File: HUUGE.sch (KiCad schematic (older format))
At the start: 16 parts

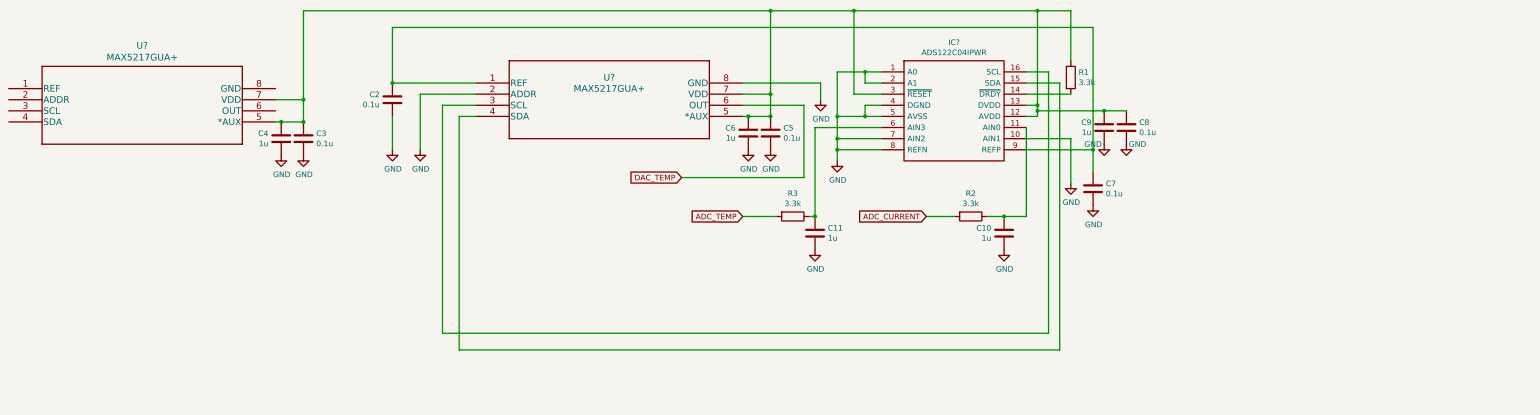
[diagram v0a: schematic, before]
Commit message: finish big sch + add appropriate labels
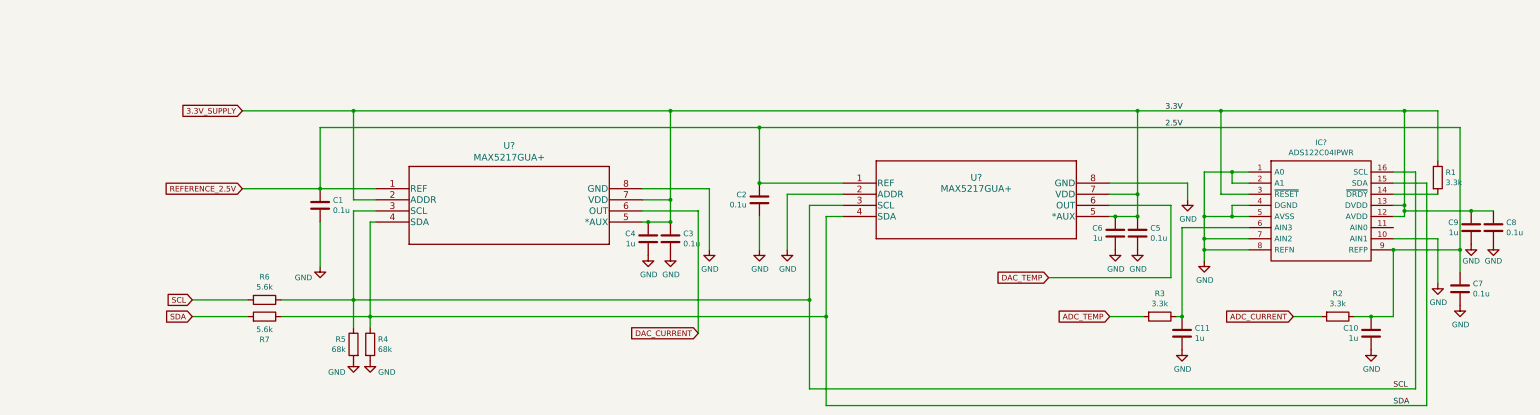
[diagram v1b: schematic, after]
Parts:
- added C1: 0.1u, symbol Device:C
- added R4, R5: 68k, symbol Device:R
- added R6, R7: 5.6k, symbol Device:R
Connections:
- net GND: now also U?.8 (GND), C1.2, R4.2, R5.2
- net REFERENCE_2.5V: now reaches C10.1, R2.1
- net REFERENCE_2.5V: now also C2.1, C7.1, IC?.9 (REFP), U?.1 (REF), U?.1 (REF), C1.1; no longer IC?.11 (AIN0)
- net 3.3V_SUPPLY: now reaches C3.1, C4.1, C5.1, C6.1, C8.1, C9.1, IC?.12 (AVDD), IC?.13 (DVDD), IC?.3 (~RESET), R1.1, U?.5 (*AUX), U?.5 (*AUX), U?.7 (VDD), U?.7 (VDD)
- net 3.3V_SUPPLY: now also U?.2 (ADDR)
- net SDA: now reaches IC?.15 (SDA), U?.4 (SDA)
- net SDA: now also U?.4 (SDA), R4.1, R7.1, R7.2
- net SCL: now reaches IC?.16 (SCL), U?.3 (SCL)
- net SCL: now also U?.3 (SCL), R5.1, R6.1, R6.2
- net DAC_CURRENT: now reaches U?.6 (OUT)
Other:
- moved on the sheet: C10, C11, C2, C3, C4, C5, C6, C7, C8, C9, IC?, R1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

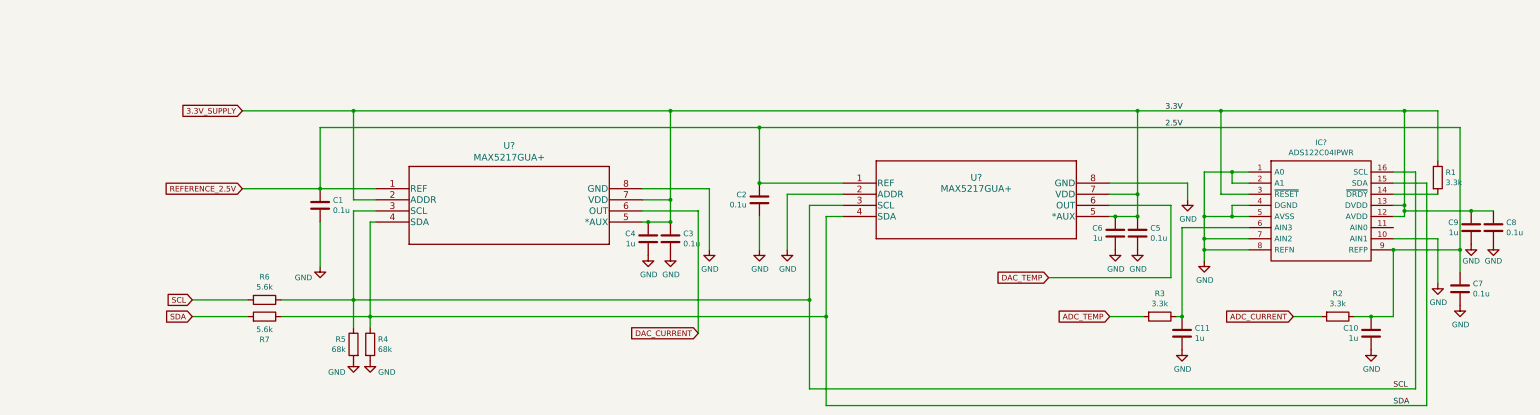
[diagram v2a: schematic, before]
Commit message: annotate all sheets
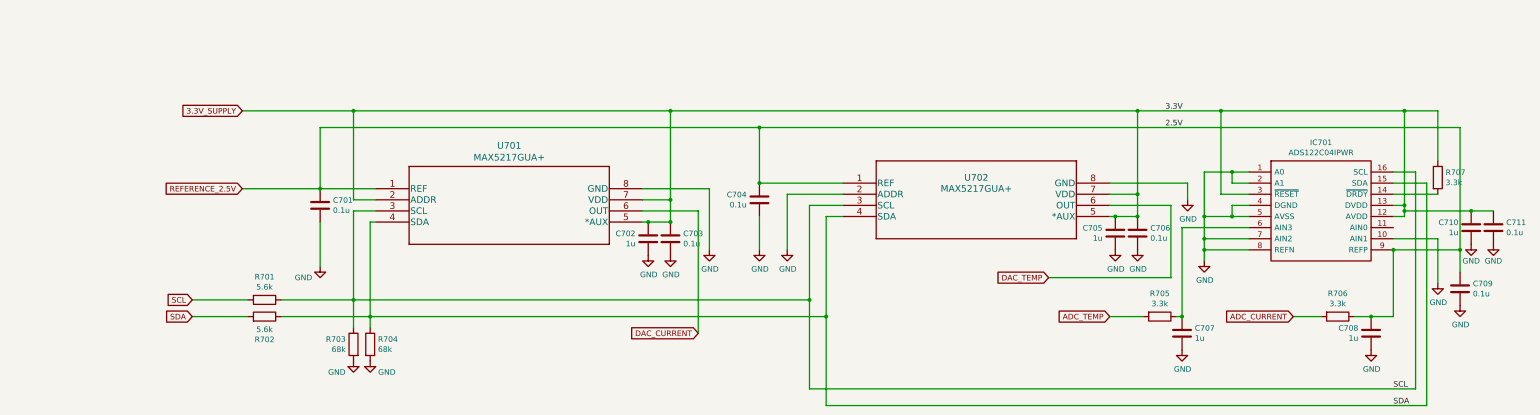
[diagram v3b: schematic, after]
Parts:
- gave numbers to parts that had none: 3
- renumbered C1 to C701, C4 to C702, C3 to C703, C2 to C704, C6 to C705, C5 to C706, C11 to C707, C10 to C708, C7 to C709, C9 to C710, C8 to C711, R6 to R701, R7 to R702, R5 to R703, R4 to R704, R3 to R705, R2 to R706, R1 to R707
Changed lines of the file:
@@
 $EndDescr
 $Comp
-L ADS122C04IPWR:ADS122C04IPWR IC?
+L ADS122C04IPWR:ADS122C04IPWR IC701
 U 1 1 60C9892C
 P 11850 4200
-F 0 "IC?" H 12500 4465 50  0000 C CNN
+F 0 "IC701" H 12500 4465 50  0000 C CNN
 F 1 "ADS122C04IPWR" H 12500 4374 50  0000 C CNN
 F 2 "SOP65P640X120-16N" H 13000 4300 50  0001 L CNN
@@
 $EndComp
 $Comp
-L MAX5217GUA:MAX5217GUA+ U?
+L MAX5217GUA:MAX5217GUA+ U701
 U 1 1 60C9B4F4
 P 4000 4350
-F 0 "U?" H 5200 4737 60  0000 C CNN
+F 0 "U701" H 5200 4737 60  0000 C CNN
 F 1 "MAX5217GUA+" H 5200 4631 60  0000 C CNN
 F 2 "21-0036K_MXM" H 5200 4590 60  0001 C CNN
@@
 $EndComp
 $Comp
-L power:GND #PWR?
+L power:GND #PWR0715
 U 1 1 60CA01ED
 P 13550 5200
-F 0 "#PWR?" H 13550 4950 50  0001 C CNN
+F 0 "#PWR0715" H 13550 4950 50  0001 C CNN
 F 1 "GND" H 13555 5027 50  0000 C CNN
 F 2 "" H 13550 5200 50  0001 C CNN
@@
 	13250 4550 13250 4500
 $Comp
-L Device:C C9
+L Device:C C710
 U 1 1 60CA1026
 P 13850 4700
-F 0 "C9" H 13735 4746 50  0000 R CNN
+F 0 "C710" H 13735 4746 50  0000 R CNN
 F 1 "1u" H 13735 4655 50  0000 R CNN
 F 2 "" H 13888 4550 50  0001 C CNN
@@
 Connection ~ 13850 4550
 $Comp
-L Device:C C8
+L Device:C C711
 U 1 1 60CA2BAA
 P 14050 4700
-F 0 "C8" H 13935 4746 50  0000 R CNN
+F 0 "C711" H 13935 4746 50  0000 R CNN
 F 1 "0.1u" H 13935 4655 50  0000 R CNN
 F 2 "" H 14088 4550 50  0001 C CNN
@@
 $EndComp
 $Comp
-L power:GND #PWR?
+L power:GND #PWR0718
 U 1 1 60CA2E29
 P 14050 4850
-F 0 "#PWR?" H 14050 4600 50  0001 C CNN
+F 0 "#PWR0718" H 14050 4600 50  0001 C CNN
 F 1 "GND" H 14050 4700 50  0000 C CNN
 F 2 "" H 14050 4850 50  0001 C CNN
@@
 	13150 4400 13550 4400
 $Comp
-L Device:R R1
+L Device:R R707
 U 1 1 60CA4AD8
 P 13550 4250
-F 0 "R1" H 13620 4296 50  0000 L CNN
+F 0 "R707" H 13620 4296 50  0000 L CNN
 F 1 "3.3k" H 13620 4205 50  0000 L CNN
 F 2 "" V 13480 4250 50  0001 C CNN
@@
 	11700 4200 11450 4200
 $Comp
-L power:GND #PWR?
+L power:GND #PWR0713
 U 1 1 60CA795D
 P 11450 5000
-F 0 "#PWR?" H 11450 4750 50  0001 C CNN
+F 0 "#PWR0713" H 11450 4750 50  0001 C CNN
 F 1 "GND" H 11455 4827 50  0000 C CNN
 F 2 "" H 11450 5000 50  0001 C CNN
@@
 	11700 4600 11450 4600
 $Comp
-L Device:C C10
+L Device:C C708
 U 1 1 60CAA79B
 P 12950 5650
-F 0 "C10" H 12835 5696 50  0000 R CNN
+F 0 "C708" H 12835 5696 50  0000 R CNN
 F 1 "1u" H 12835 5605 50  0000 R CNN
 F 2 "" H 12988 5500 50  0001 C CNN
@@
 	12950 5500 12800 5500
 $Comp
-L Device:R R2
+L Device:R R706
 U 1 1 60CAB097
 P 12650 5500
-F 0 "R2" V 12443 5500 50  0000 C CNN
+F 0 "R706" V 12443 5500 50  0000 C CNN
 F 1 "3.3k" V 12534 5500 50  0000 C CNN
 F 2 "" V 12580 5500 50  0001 C CNN
@@
 ADC_CURRENT
 $Comp
-L power:GND #PWR?
+L power:GND #PWR0714
 U 1 1 60CAB8DE
 P 12950 5800
-F 0 "#PWR?" H 12950 5550 50  0001 C CNN
+F 0 "#PWR0714" H 12950 5550 50  0001 C CNN
 F 1 "GND" H 12955 5627 50  0000 C CNN
 F 2 "" H 12950 5800 50  0001 C CNN
@@
 $EndComp
 $Comp
-L power:GND #PWR?
+L power:GND #PWR0717
 U 1 1 60CA15DB
 P 13850 4850
-F 0 "#PWR?" H 13850 4600 50  0001 C CNN
+F 0 "#PWR0717" H 13850 4600 50  0001 C CNN
 F 1 "GND" H 13850 4700 50  0000 C CNN
 F 2 "" H 13850 4850 50  0001 C CNN
@@
 $EndComp
 $Comp
-L power:GND #PWR?
+L power:GND #PWR0716
 U 1 1 60C9FA7D
 P 13750 5400
-F 0 "#PWR?" H 13750 5150 50  0001 C CNN
+F 0 "#PWR0716" H 13750 5150 50  0001 C CNN
 F 1 "GND" H 13755 5227 50  0000 C CNN
 F 2 "" H 13750 5400 50  0001 C CNN
@@
 $EndComp
 $Comp
-L Device:C C7
+L Device:C C709
 U 1 1 60C9F129
 P 13750 5250
-F 0 "C7" H 13865 5296 50  0000 L CNN
+F 0 "C709" H 13865 5296 50  0000 L CNN
 F 1 "0.1u" H 13865 5205 50  0000 L CNN
 F 2 "" H 13788 5100 50  0001 C CNN
@@
 	11250 4700 11250 5500
 $Comp
-L power:GND #PWR?
+L power:GND #PWR0711
 U 1 1 60CB388F
 P 11250 5800
-F 0 "#PWR?" H 11250 5550 50  0001 C CNN
+F 0 "#PWR0711" H 11250 5550 50  0001 C CNN
 F 1 "GND" H 11255 5627 50  0000 C CNN
 F 2 "" H 11250 5800 50  0001 C CNN
@@
 Connection ~ 11250 5500
 $Comp
-L Device:C C11
+L Device:C C707
 U 1 1 60CB2B9B
 P 11250 5650
-F 0 "C11" H 11365 5696 50  0000 L CNN
+F 0 "C707" H 11365 5696 50  0000 L CNN
 F 1 "1u" H 11365 5605 50  0000 L CNN
 F 2 "" H 11288 5500 50  0001 C CNN
@@
 $EndComp
 $Comp
-L Device:R R3
+L Device:R R705
 U 1 1 60CB4FA3
 P 11050 5500
-F 0 "R3" V 10843 5500 50  0000 C CNN
+F 0 "R705" V 10843 5500 50  0000 C CNN
 F 1 "3.3k" V 10934 5500 50  0000 C CNN
 F 2 "" V 10980 5500 50  0001 C CNN
@@
 Connection ~ 11600 3650
 $Comp
-L Device:C C5
+L Device:C C706
 U 1 1 60CB8424
 P 10850 4750
-F 0 "C5" H 10965 4796 50  0000 L CNN
+F 0 "C706" H 10965 4796 50  0000 L CNN
 F 1 "0.1u" H 10965 4705 50  0000 L CNN
 F 2 "" H 10888 4600 50  0001 C CNN
@@
 $EndComp
 $Comp
-L Device:C C6
+L Device:C C705
 U 1 1 60CB8CAB
 P 10650 4750
-F 0 "C6" H 10765 4796 50  0000 L CNN
+F 0 "C705" H 10765 4796 50  0000 L CNN
 F 1 "1u" H 10765 4705 50  0000 L CNN
 F 2 "" H 10688 4600 50  0001 C CNN
@@
 $EndComp
 $Comp
-L MAX5217GUA:MAX5217GUA+ U?
+L MAX5217GUA:MAX5217GUA+ U702
 U 1 1 60C9AC5D
 P 8200 4300
-F 0 "U?" H 9400 4350 60  0000 C CNN
+F 0 "U702" H 9400 4350 60  0000 C CNN
 F 1 "MAX5217GUA+" H 9400 4250 60  0000 C CNN
 F 2 "21-0036K_MXM" H 9400 4540 60  0001 C CNN
@@
 $EndComp
 $Comp
-L power:GND #PWR?
+L power:GND #PWR0709
 U 1 1 60CBD459
 P 10650 4900
-F 0 "#PWR?" H 10650 4650 50  0001 C CNN
+F 0 "#PWR0709" H 10650 4650 50  0001 C CNN
 F 1 "GND" H 10655 4727 50  0000 C CNN
 F 2 "" H 10650 4900 50  0001 C CNN
@@
 $EndComp
 $Comp
-L power:GND #PWR?
+L power:GND #PWR0710
 U 1 1 60CBD86E
 P 10850 4900
-F 0 "#PWR?" H 10850 4650 50  0001 C CNN
+F 0 "#PWR0710" H 10850 4650 50  0001 C CNN
 F 1 "GND" H 10855 4727 50  0000 C CNN
 F 2 "" H 10850 4900 50  0001 C CNN
@@
 	10600 4400 10850 4400
 $Comp
-L power:GND #PWR?
+L power:GND #PWR0712
 U 1 1 60CCEF62
 P 11300 4450
-F 0 "#PWR?" H 11300 4200 50  0001 C CNN
+F 0 "#PWR0712" H 11300 4200 50  0001 C CNN
 F 1 "GND" H 11305 4277 50  0000 C CNN
 F 2 "" H 11300 4450 50  0001 C CNN
@@
 	7450 3800 13750 3800
 $Comp
-L power:GND #PWR?
+L power:GND #PWR0707
 U 1 1 60CF506B
 P 7450 4900
-F 0 "#PWR?" H 7450 4650 50  0001 C CNN
+F 0 "#PWR0707" H 7450 4650 50  0001 C CNN
 F 1 "GND" H 7455 4727 50  0000 C CNN
 F 2 "" H 7450 4900 50  0001 C CNN
@@
 	8200 4300 7450 4300
 $Comp
-L Device:C C2
+L Device:C C704
 U 1 1 60CF22BC
 P 7450 4450
-F 0 "C2" H 7565 4496 50  0000 L CNN
+F 0 "C704" H 7565 4496 50  0000 L CNN
 F 1 "0.1u" H 7565 4405 50  0000 L CNN
 F 2 "" H 7488 4300 50  0001 C CNN
@@
 	7700 4400 7700 4900
 $Comp
-L power:GND #PWR?
+L power:GND #PWR0708
 U 1 1 60D35967
 P 7700 4900
-F 0 "#PWR?" H 7700 4650 50  0001 C CNN
+F 0 "#PWR0708" H 7700 4650 50  0001 C CNN
 F 1 "GND" H 7705 4727 50  0000 C CNN
 F 2 "" H 7700 4900 50  0001 C CNN
@@
 Connection ~ 7450 4300
 $Comp
-L Device:C C3
+L Device:C C703
 U 1 1 60D3E32C
 P 6650 4800
-F 0 "C3" H 6765 4846 50  0000 L CNN
+F 0 "C703" H 6765 4846 50  0000 L CNN
 F 1 "0.1u" H 6765 4755 50  0000 L CNN
 F 2 "" H 6688 4650 50  0001 C CNN
@@
 $EndComp
 $Comp
-L power:GND #PWR?
+L power:GND #PWR0704
 U 1 1 60D3E340
 P 6450 4950
-F 0 "#PWR?" H 6450 4700 50  0001 C CNN
+F 0 "#PWR0704" H 6450 4700 50  0001 C CNN
 F 1 "GND" H 6455 4777 50  0000 C CNN
 F 2 "" H 6450 4950 50  0001 C CNN
@@
 $EndComp
 $Comp
-L power:GND #PWR?
+L power:GND #PWR0705
 U 1 1 60D3E34A
 P 6650 4950
-F 0 "#PWR?" H 6650 4700 50  0001 C CNN
+F 0 "#PWR0705" H 6650 4700 50  0001 C CNN
 F 1 "GND" H 6655 4777 50  0000 C CNN
 F 2 "" H 6650 4950 50  0001 C CNN
@@
 	6400 4650 6450 4650
 $Comp
-L Device:C C4
+L Device:C C702
 U 1 1 60D3E336
 P 6450 4800
-F 0 "C4" H 6335 4846 50  0000 R CNN
+F 0 "C702" H 6335 4846 50  0000 R CNN
 F 1 "1u" H 6335 4755 50  0000 R CNN
 F 2 "" H 6488 4650 50  0001 C CNN
@@
 	7000 4350 7000 4900
 $Comp
-L power:GND #PWR?
+L power:GND #PWR0706
 U 1 1 60D628E4
 P 7000 4900
-F 0 "#PWR?" H 7000 4650 50  0001 C CNN
+F 0 "#PWR0706" H 7000 4650 50  0001 C CNN
 F 1 "GND" H 7005 4727 50  0000 C CNN
 F 2 "" H 7000 4900 50  0001 C CNN
@@
 REFERENCE_2.5V
 $Comp
-L Device:C C1
+L Device:C C701
 U 1 1 60D9820C
 P 3500 4500
-F 0 "C1" H 3615 4546 50  0000 L CNN
+F 0 "C701" H 3615 4546 50  0000 L CNN
 F 1 "0.1u" H 3615 4455 50  0000 L CNN
 F 2 "" H 3538 4350 50  0001 C CNN
@@
 	3950 5500 3950 5600
 $Comp
-L Device:R R5
+L Device:R R703
 U 1 1 60DB0507
 P 3800 5750
-F 0 "R5" H 3870 5796 50  0000 L CNN
+F 0 "R703" H 3870 5796 50  0000 L CNN
 F 1 "68k" H 3870 5705 50  0000 L CNN
 F 2 "" V 3730 5750 50  0001 C CNN
@@
 $EndComp
 $Comp
-L Device:R R4
+L Device:R R704
 U 1 1 60DB434D
 P 3950 5750
-F 0 "R4" H 4020 5796 50  0000 L CNN
+F 0 "R704" H 4020 5796 50  0000 L CNN
 F 1 "68k" H 4020 5705 50  0000 L CNN
 F 2 "" V 3880 5750 50  0001 C CNN
@@
 $EndComp
 $Comp
-L power:GND #PWR?
+L power:GND #PWR0702
 U 1 1 60DB49EA
 P 3800 5900
-F 0 "#PWR?" H 3800 5650 50  0001 C CNN
+F 0 "#PWR0702" H 3800 5650 50  0001 C CNN
 F 1 "GND" H 3650 5800 50  0000 C CNN
 F 2 "" H 3800 5900 50  0001 C CNN
@@
 $EndComp
 $Comp
-L power:GND #PWR?
+L power:GND #PWR0703
 U 1 1 60DB50A1
 P 3950 5900
-F 0 "#PWR?" H 3950 5650 50  0001 C CNN
+F 0 "#PWR0703" H 3950 5650 50  0001 C CNN
 F 1 "GND" H 4100 5800 50  0000 C CNN
 F 2 "" H 3950 5900 50  0001 C CNN
@@
 $EndComp
 $Comp
-L power:GND #PWR?
+L power:GND #PWR0701
 U 1 1 60DB5776
 P 3500 5050
-F 0 "#PWR?" H 3500 4800 50  0001 C CNN
+F 0 "#PWR0701" H 3500 4800 50  0001 C CNN
 F 1 "GND" H 3350 4950 50  0000 C CNN
 F 2 "" H 3500 5050 50  0001 C CNN
@@
 $EndComp
 $Comp
-L Device:R R6
+L Device:R R701
 U 1 1 60DB5FD8
 P 3000 5350
-F 0 "R6" V 2793 5350 50  0000 C CNN
+F 0 "R701" V 2793 5350 50  0000 C CNN
 F 1 "5.6k" V 2884 5350 50  0000 C CNN
 F 2 "" V 2930 5350 50  0001 C CNN
@@
 $EndComp
 $Comp
-L Device:R R7
+L Device:R R702
 U 1 1 60DB6550
 P 3000 5500
-F 0 "R7" V 2793 5500 50  0000 C CNN
+F 0 "R702" V 2793 5500 50  0000 C CNN
 F 1 "5.6k" V 2884 5500 50  0000 C CNN
 F 2 "" V 2930 5500 50  0001 C CNN

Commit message: add footprints julia
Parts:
- IC701: footprint SOP65P640X120-16N -> footprint libraries:ADS122C04IPWR
- U701, U702: footprint 21-0036K_MXM -> footprint libraries:MAX5217GUA&plus_
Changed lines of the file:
@@
 F 0 "IC701" H 12500 4465 50  0000 C CNN
 F 1 "ADS122C04IPWR" H 12500 4374 50  0000 C CNN
-F 2 "SOP65P640X120-16N" H 13000 4300 50  0001 L CNN
+F 2 "footprint libraries:ADS122C04IPWR" H 13000 4300 50  0001 L CNN
 F 3 "http://www.ti.com/lit/gpn/ads122c04" H 13000 4200 50  0001 L CNN
 F 4 "Analog to Digital Converters - ADC 24-Bit, 2kSPS, 4-Ch, Low-Power Delta-Sigma ADC With PGA, Voltage Reference, IDACs and I2C Interface 16-TSSOP -40 to 125" H 13000 4100 50  0001 L CNN "Description"
@@
 F 0 "U701" H 5200 4737 60  0000 C CNN
 F 1 "MAX5217GUA+" H 5200 4631 60  0000 C CNN
-F 2 "21-0036K_MXM" H 5200 4590 60  0001 C CNN
+F 2 "footprint libraries:MAX5217GUA&plus_" H 5200 4590 60  0001 C CNN
 F 3 "" H 4000 4350 60  0000 C CNN
 	1    4000 4350
@@
 F 0 "U702" H 9400 4350 60  0000 C CNN
 F 1 "MAX5217GUA+" H 9400 4250 60  0000 C CNN
-F 2 "21-0036K_MXM" H 9400 4540 60  0001 C CNN
+F 2 "footprint libraries:MAX5217GUA&plus_" H 9400 4540 60  0001 C CNN
 F 3 "" H 8200 4300 60  0000 C CNN
 	1    8200 4300

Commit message: added vishay dude & capacitor & resistor footprints
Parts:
- C701, C702, C703, C704, C705, C706, C707, C708, C709, C710, C711: footprint (none) -> Capacitor_SMD:C_0402_1005Metric
- R701, R702, R703, R704, R705, R706, R707: footprint (none) -> Resistor_SMD:R_0402_1005Metric
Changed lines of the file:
@@
 F 0 "C710" H 13735 4746 50  0000 R CNN
 F 1 "1u" H 13735 4655 50  0000 R CNN
-F 2 "" H 13888 4550 50  0001 C CNN
+F 2 "Capacitor_SMD:C_0402_1005Metric" H 13888 4550 50  0001 C CNN
 F 3 "~" H 13850 4700 50  0001 C CNN
 	1    13850 4700
@@
 F 0 "C711" H 13935 4746 50  0000 R CNN
 F 1 "0.1u" H 13935 4655 50  0000 R CNN
-F 2 "" H 14088 4550 50  0001 C CNN
+F 2 "Capacitor_SMD:C_0402_1005Metric" H 14088 4550 50  0001 C CNN
 F 3 "~" H 14050 4700 50  0001 C CNN
 	1    14050 4700
@@
 F 0 "R707" H 13620 4296 50  0000 L CNN
 F 1 "3.3k" H 13620 4205 50  0000 L CNN
-F 2 "" V 13480 4250 50  0001 C CNN
+F 2 "Resistor_SMD:R_0402_1005Metric" V 13480 4250 50  0001 C CNN
 F 3 "~" H 13550 4250 50  0001 C CNN
 	1    13550 4250
@@
 F 0 "C708" H 12835 5696 50  0000 R CNN
 F 1 "1u" H 12835 5605 50  0000 R CNN
-F 2 "" H 12988 5500 50  0001 C CNN
+F 2 "Capacitor_SMD:C_0402_1005Metric" H 12988 5500 50  0001 C CNN
 F 3 "~" H 12950 5650 50  0001 C CNN
 	1    12950 5650
@@
 F 0 "R706" V 12443 5500 50  0000 C CNN
 F 1 "3.3k" V 12534 5500 50  0000 C CNN
-F 2 "" V 12580 5500 50  0001 C CNN
+F 2 "Resistor_SMD:R_0402_1005Metric" V 12580 5500 50  0001 C CNN
 F 3 "~" H 12650 5500 50  0001 C CNN
 	1    12650 5500
@@
 F 0 "C709" H 13865 5296 50  0000 L CNN
 F 1 "0.1u" H 13865 5205 50  0000 L CNN
-F 2 "" H 13788 5100 50  0001 C CNN
+F 2 "Capacitor_SMD:C_0402_1005Metric" H 13788 5100 50  0001 C CNN
 F 3 "~" H 13750 5250 50  0001 C CNN
 	1    13750 5250
@@
 F 0 "C707" H 11365 5696 50  0000 L CNN
 F 1 "1u" H 11365 5605 50  0000 L CNN
-F 2 "" H 11288 5500 50  0001 C CNN
+F 2 "Capacitor_SMD:C_0402_1005Metric" H 11288 5500 50  0001 C CNN
 F 3 "~" H 11250 5650 50  0001 C CNN
 	1    11250 5650
@@
 F 0 "R705" V 10843 5500 50  0000 C CNN
 F 1 "3.3k" V 10934 5500 50  0000 C CNN
-F 2 "" V 10980 5500 50  0001 C CNN
+F 2 "Resistor_SMD:R_0402_1005Metric" V 10980 5500 50  0001 C CNN
 F 3 "~" H 11050 5500 50  0001 C CNN
 	1    11050 5500
@@
 F 0 "C706" H 10965 4796 50  0000 L CNN
 F 1 "0.1u" H 10965 4705 50  0000 L CNN
-F 2 "" H 10888 4600 50  0001 C CNN
+F 2 "Capacitor_SMD:C_0402_1005Metric" H 10888 4600 50  0001 C CNN
 F 3 "~" H 10850 4750 50  0001 C CNN
 	1    10850 4750
@@
 F 0 "C705" H 10765 4796 50  0000 L CNN
 F 1 "1u" H 10765 4705 50  0000 L CNN
-F 2 "" H 10688 4600 50  0001 C CNN
+F 2 "Capacitor_SMD:C_0402_1005Metric" H 10688 4600 50  0001 C CNN
 F 3 "~" H 10650 4750 50  0001 C CNN
 	1    10650 4750
@@
 F 0 "C704" H 7565 4496 50  0000 L CNN
 F 1 "0.1u" H 7565 4405 50  0000 L CNN
-F 2 "" H 7488 4300 50  0001 C CNN
+F 2 "Capacitor_SMD:C_0402_1005Metric" H 7488 4300 50  0001 C CNN
 F 3 "~" H 7450 4450 50  0001 C CNN
 	1    7450 4450
@@
 F 0 "C703" H 6765 4846 50  0000 L CNN
 F 1 "0.1u" H 6765 4755 50  0000 L CNN
-F 2 "" H 6688 4650 50  0001 C CNN
+F 2 "Capacitor_SMD:C_0402_1005Metric" H 6688 4650 50  0001 C CNN
 F 3 "~" H 6650 4800 50  0001 C CNN
 	1    6650 4800
@@
 F 0 "C702" H 6335 4846 50  0000 R CNN
 F 1 "1u" H 6335 4755 50  0000 R CNN
-F 2 "" H 6488 4650 50  0001 C CNN
+F 2 "Capacitor_SMD:C_0402_1005Metric" H 6488 4650 50  0001 C CNN
 F 3 "~" H 6450 4800 50  0001 C CNN
 	1    6450 4800
@@
 F 0 "C701" H 3615 4546 50  0000 L CNN
 F 1 "0.1u" H 3615 4455 50  0000 L CNN
-F 2 "" H 3538 4350 50  0001 C CNN
+F 2 "Capacitor_SMD:C_0402_1005Metric" H 3538 4350 50  0001 C CNN
 F 3 "~" H 3500 4500 50  0001 C CNN
 	1    3500 4500
@@
 F 0 "R703" H 3870 5796 50  0000 L CNN
 F 1 "68k" H 3870 5705 50  0000 L CNN
-F 2 "" V 3730 5750 50  0001 C CNN
+F 2 "Resistor_SMD:R_0402_1005Metric" V 3730 5750 50  0001 C CNN
 F 3 "~" H 3800 5750 50  0001 C CNN
 	1    3800 5750
@@
 F 0 "R704" H 4020 5796 50  0000 L CNN
 F 1 "68k" H 4020 5705 50  0000 L CNN
-F 2 "" V 3880 5750 50  0001 C CNN
+F 2 "Resistor_SMD:R_0402_1005Metric" V 3880 5750 50  0001 C CNN
 F 3 "~" H 3950 5750 50  0001 C CNN
 	1    3950 5750
@@
 F 0 "R701" V 2793 5350 50  0000 C CNN
 F 1 "5.6k" V 2884 5350 50  0000 C CNN
-F 2 "" V 2930 5350 50  0001 C CNN
+F 2 "Resistor_SMD:R_0402_1005Metric" V 2930 5350 50  0001 C CNN
 F 3 "~" H 3000 5350 50  0001 C CNN
 	1    3000 5350
@@
 F 0 "R702" V 2793 5500 50  0000 C CNN
 F 1 "5.6k" V 2884 5500 50  0000 C CNN
-F 2 "" V 2930 5500 50  0001 C CNN
+F 2 "Resistor_SMD:R_0402_1005Metric" V 2930 5500 50  0001 C CNN
 F 3 "~" H 3000 5500 50  0001 C CNN
 	1    3000 5500

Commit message: pushing all changes and ports
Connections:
- net 3.3V_SUPPLY renamed 3.3V
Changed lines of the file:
@@
 Connection ~ 3800 3650
 Text GLabel 2800 3650 0    50   Input ~ 0
-3.3V_SUPPLY
+3.3V
 Wire Wire Line
 	4000 4350 3500 4350

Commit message: keep on adding global labels
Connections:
- net ADC_TEMP renamed Therm_to_AtoD
- net DAC_TEMP renamed DtoA_Output_(Setpoint)
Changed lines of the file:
@@
 	10900 5500 10600 5500
 Text GLabel 10600 5500 0    50   Input ~ 0
-ADC_TEMP
+Therm_to_AtoD
 Wire Wire Line
 	10850 3650 11600 3650
@@
 	10600 4500 11150 4500
 Text GLabel 10050 5150 0    50   Input ~ 0
-DAC_TEMP
+DtoA_Output_(Setpoint)
 Wire Wire Line
 	10600 4400 10850 4400
